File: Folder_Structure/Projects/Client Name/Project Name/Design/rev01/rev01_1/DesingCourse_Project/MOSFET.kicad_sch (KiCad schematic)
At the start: 0 parts

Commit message: Update 6
SCH and LIB for MOSFET page done, missing passive components
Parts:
- added C42, C43: 2n2, symbol Device:C
- added J4, J5, J6: 7461084, WP-BUTR:WP-BUTR_7461084, symbol 7461084:WP-7461084
- added NT2, NT3, NT4, NT5: NetTie_2, symbol Device:NetTie_2
- added Q1, Q2, Q3, Q4, Q5, Q6: HSBA15810C, Package_SO:PowerPAK_SO-8_Single, symbol HSBA15810C:HSBA15810C
- added R24, R26, R30, R31, R36, R37: 4R7, symbol Device:R
- added R25, R32, R38: 39K, symbol Device:R
- added R27, R28, R33, R34: 100, symbol Device:R
- added R29, R35: 1m, RES_WSLP2726L5000FEA:WSLP2726_1mOHM_VIS, symbol WSLP27261L000FEA:WSLP27261L000FEA
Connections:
- new net +VDC: Q1.5 (D), Q3.5 (D), Q5.5 (D)
- new net GND: NT5.1, R25.2, R29.2, R32.2, R35.2, R38.2
- new net H1_LOW: Q2.1 (S), Q2.2 (S), Q2.3 (S), R29.1
- new net H1_VS: NT2.1
- new net H2_LOW: Q4.1 (S), Q4.2 (S), Q4.3 (S), R35.1
- new net H2_VS: NT3.1
- new net H3_LOW: NT5.2, Q6.1 (S), Q6.2 (S), Q6.3 (S)
- new net H3_VS: NT4.1
- new net M_H1: R24.1
- new net M_H1_RG: Q1.4 (G), R24.2
- new net M_H2: R30.1
- new net M_H2_RG: Q3.4 (G), R30.2
- new net M_H3: R36.1
- new net M_H3_RG: Q5.4 (G), R36.2
- new net M_L1: R26.1
- new net M_L1_RG: Q2.4 (G), R25.1, R26.2
- new net M_L2: R31.1
- new net M_L2_RG: Q4.4 (G), R31.2, R32.1
- new net M_L3: R37.1
- new net M_L3_RG: Q6.4 (G), R37.2, R38.1
- new net PHASE_1: J4.1, J4.2, J4.3, J4.4, J4.5, J4.6, J4.7, J4.8, NT2.2, Q1.1 (S), Q1.2 (S), Q1.3 (S), Q2.5 (D)
- new net PHASE_2: J5.1, J5.2, J5.3, J5.4, J5.5, J5.6, J5.7, J5.8, NT3.2, Q3.1 (S), Q3.2 (S), Q3.3 (S), Q4.5 (D)
- new net PHASE_3: J6.1, J6.2, J6.3, J6.4, J6.5, J6.6, J6.7, J6.8, NT4.2, Q5.1 (S), Q5.2 (S), Q5.3 (S), Q6.5 (D)
- new net S1_N: C42.1, R27.1
- new net S1_P: C42.2, R28.1
- new net S2_N: C43.1, R33.1
- new net S2_P: C43.2, R34.1
- new net SH1_N: R27.2, R29.3
- new net SH1_P: R28.2, R29.4
- new net SH2_N: R33.2, R35.3
- new net SH2_P: R34.2, R35.4
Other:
- note added: "H#_VS"
- note added: "Kelving connection for sensing"
- note added: "M6 screw terminal"
- note added: "MCU SENSING FEEDBACK FOR EACH PHASE"
- note added: "MOSFETs"
- note added: "OUTPUT PHASE 1"
- note added: "OUTPUT PHASE 2"
- note added: "OUTPUT PHASE 3"
- note added: "Phase 1"
- note added: "Phase 2"
- note added: "Phase 3"
- note added: "Place as close as possible to the bulk capacitanace"
- note added: "Q_CONTROL"
- note added: "Q_SOURCES"
- note added: "SENSE L1"
- note added: "SENSE L2"
- company: (none) -> Integro Consulting AB
- title: (none) -> PCB Mastery Project

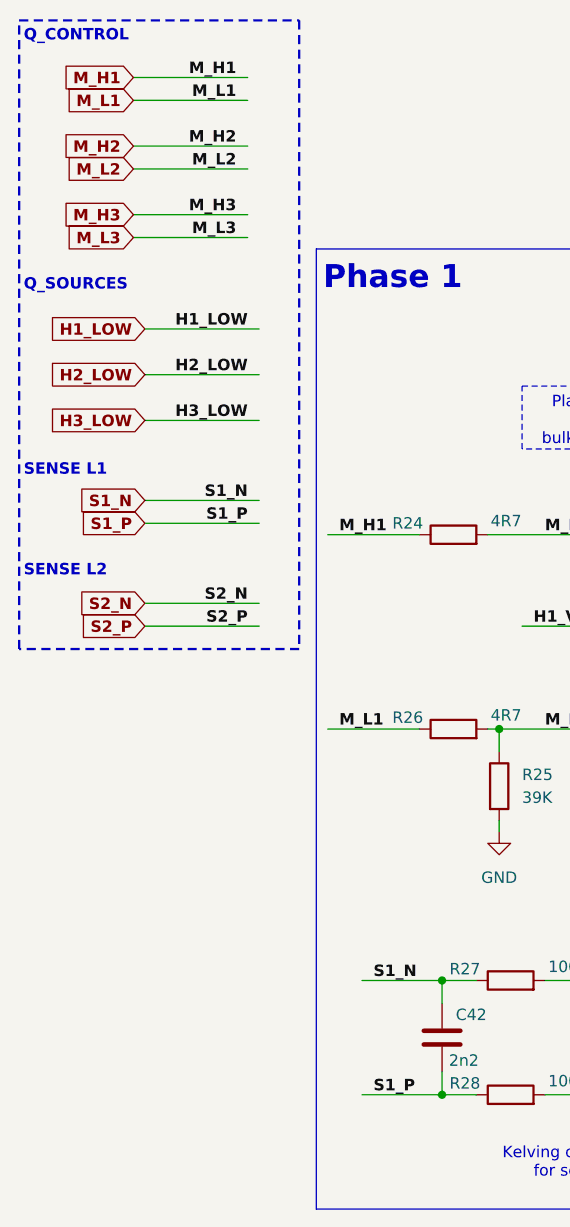
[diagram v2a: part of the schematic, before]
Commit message: Update 10
All done up to MOSFET page, replace all connected to actual PN
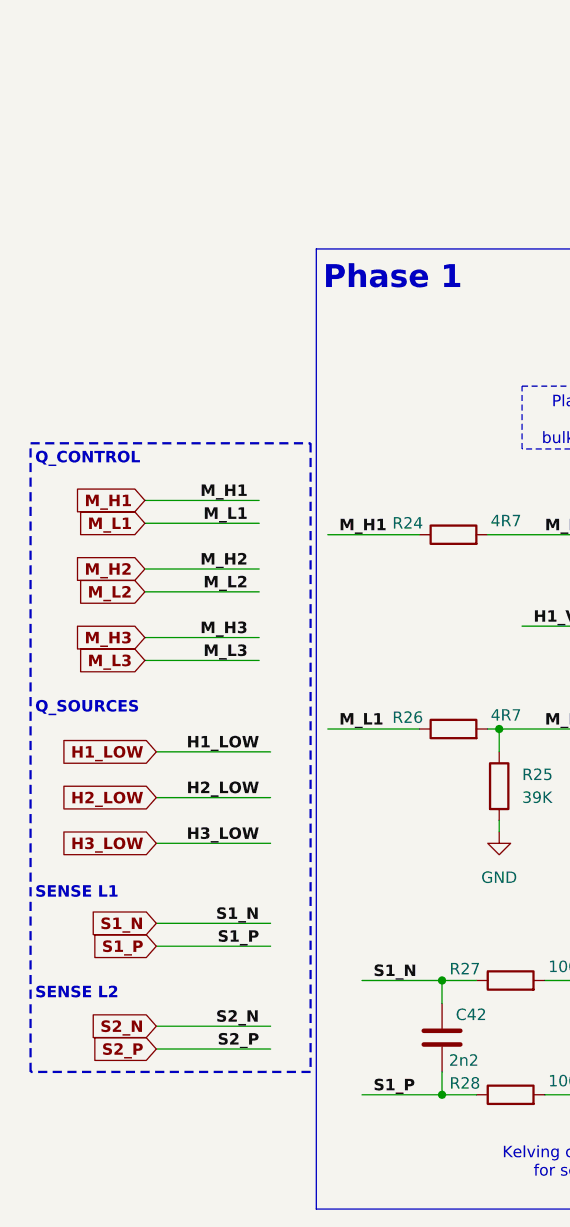
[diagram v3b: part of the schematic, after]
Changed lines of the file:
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@@
 	)
 	(rectangle
-		(start 12.7 12.7)
-		(end 43.815 82.55)
+		(start 13.97 59.69)
+		(end 45.085 129.54)
 		(stroke
 			(width 0.254)
@@
 	(text "Q_CONTROL"
 		(exclude_from_sim no)
-		(at 13.208 14.478 0)
+		(at 14.478 61.468 0)
 		(effects
 			(font
@@
 	(text "Q_SOURCES\n"
 		(exclude_from_sim no)
-		(at 13.208 42.164 0)
+		(at 14.478 89.154 0)
 		(effects
 			(font
@@
 	(text "SENSE L1"
 		(exclude_from_sim no)
-		(at 13.208 62.738 0)
+		(at 14.478 109.728 0)
 		(effects
 			(font
@@
 	(text "SENSE L2\n"
 		(exclude_from_sim no)
-		(at 13.208 73.914 0)
+		(at 14.478 120.904 0)
 		(effects
 			(font
@@
 	(wire
 		(pts
-			(xy 39.37 66.04) (xy 26.67 66.04)
+			(xy 40.64 113.03) (xy 27.94 113.03)
 		)
 		(stroke
@@
 	(wire
 		(pts
-			(xy 38.1 26.67) (xy 25.4 26.67)
+			(xy 39.37 73.66) (xy 26.67 73.66)
 		)
 		(stroke
@@
 	(wire
 		(pts
-			(xy 38.1 21.59) (xy 25.4 21.59)
+			(xy 39.37 68.58) (xy 26.67 68.58)
 		)
 		(stroke
@@
 	(wire
 		(pts
-			(xy 38.1 19.05) (xy 25.4 19.05)
+			(xy 39.37 66.04) (xy 26.67 66.04)
 		)
 		(stroke
@@
 	(wire
 		(pts
-			(xy 39.37 57.15) (xy 26.67 57.15)
+			(xy 40.64 104.14) (xy 27.94 104.14)
 		)
 		(stroke
@@
 	(wire
 		(pts
-			(xy 39.37 46.99) (xy 26.67 46.99)
+			(xy 40.64 93.98) (xy 27.94 93.98)
 		)
 		(stroke
@@
 	(wire
 		(pts
-			(xy 39.37 68.58) (xy 26.67 68.58)
+			(xy 40.64 115.57) (xy 27.94 115.57)
 		)
 		(stroke
@@
 	(wire
 		(pts
-			(xy 38.1 29.21) (xy 25.4 29.21)
+			(xy 39.37 76.2) (xy 26.67 76.2)
 		)
 		(stroke
@@
 	(wire
 		(pts
-			(xy 38.1 34.29) (xy 25.4 34.29)
+			(xy 39.37 81.28) (xy 26.67 81.28)
 		)
 		(stroke
@@
 	(wire
 		(pts
-			(xy 39.37 77.47) (xy 26.67 77.47)
+			(xy 40.64 124.46) (xy 27.94 124.46)
 		)
 		(stroke
@@
 	(wire
 		(pts
-			(xy 39.37 52.07) (xy 26.67 52.07)
+			(xy 40.64 99.06) (xy 27.94 99.06)
 		)
 		(stroke
@@
 	(wire
 		(pts
-			(xy 38.1 36.83) (xy 25.4 36.83)
+			(xy 39.37 83.82) (xy 26.67 83.82)
 		)
 		(stroke
@@
 	(wire
 		(pts
-			(xy 39.37 80.01) (xy 26.67 80.01)
+			(xy 40.64 127) (xy 27.94 127)
 		)
 		(stroke
@@
 	)
 	(label "H2_LOW"
-		(at 38.1 52.07 180)
+		(at 39.37 99.06 180)
 		(effects
 			(font
@@
 	)
 	(label "M_L1"
-		(at 36.83 21.59 180)
+		(at 38.1 68.58 180)
 		(effects
 			(font
@@
 	)
 	(label "H3_LOW"
-		(at 38.1 57.15 180)
+		(at 39.37 104.14 180)
 		(effects
 			(font
@@
 	)
 	(label "M_H1"
-		(at 36.83 19.05 180)
+		(at 38.1 66.04 180)
 		(effects
 			(font
@@
 	)
 	(label "S1_N"
-		(at 38.1 66.04 180)
+		(at 39.37 113.03 180)
 		(effects
 			(font
@@
 	)
 	(label "S2_N"
-		(at 38.1 77.47 180)
+		(at 39.37 124.46 180)
 		(effects
 			(font
@@
 	)
 	(label "S2_P"
-		(at 38.1 80.01 180)
+		(at 39.37 127 180)
 		(effects
 			(font
@@
 	)
 	(label "M_H2"
-		(at 36.83 26.67 180)
+		(at 38.1 73.66 180)
 		(effects
 			(font
@@
 	)
 	(label "M_H3"
-		(at 36.83 34.29 180)
+		(at 38.1 81.28 180)
 		(effects
 			(font
@@
 	)
 	(label "M_L3"
-		(at 36.83 36.83 180)
+		(at 38.1 83.82 180)
 		(effects
 			(font
@@
 	)
 	(label "H1_LOW"
-		(at 38.1 46.99 180)
+		(at 39.37 93.98 180)
 		(effects
 			(font
@@
 	)
 	(label "S1_P"
-		(at 38.1 68.58 180)
+		(at 39.37 115.57 180)
 		(effects
 			(font
@@
 	)
 	(label "M_L2"
-		(at 36.83 29.21 180)
+		(at 38.1 76.2 180)
 		(effects
 			(font
@@
 	(global_label "M_L1"
 		(shape input)
-		(at 25.4 21.59 180)
+		(at 26.67 68.58 180)
 		(fields_autoplaced yes)
 		(effects
@@
 		)
 		(property "Intersheetrefs" "${INTERSHEET_REFS}"
-			(at 17.1871 21.59 0)
+			(at 18.4571 68.58 0)
 			(effects
 				(font
@@
 	(global_label "S2_P"
 		(shape input)
-		(at 26.67 80.01 180)
+		(at 27.94 127 180)
 		(fields_autoplaced yes)
 		(effects
@@
 		)
 		(property "Intersheetrefs" "${INTERSHEET_REFS}"
-			(at 18.4571 80.01 0)
+			(at 19.7271 127 0)
 			(effects
 				(font
@@
 	(global_label "H2_LOW"
 		(shape input)
-		(at 26.67 52.07 180)
+		(at 27.94 99.06 180)
 		(fields_autoplaced yes)
 		(effects
@@
 		)
 		(property "Intersheetrefs" "${INTERSHEET_REFS}"
-			(at 15.7961 52.07 0)
+			(at 17.0661 99.06 0)
 			(effects
 				(font
@@
 	(global_label "M_H3"
 		(shape input)
-		(at 25.4 34.29 180)
+		(at 26.67 81.28 180)
 		(fields_autoplaced yes)
 		(effects
@@
 		)
 		(property "Intersheetrefs" "${INTERSHEET_REFS}"
-			(at 16.8847 34.29 0)
+			(at 18.1547 81.28 0)
 			(effects
 				(font
@@
 	(global_label "H3_LOW"
 		(shape input)
-		(at 26.67 57.15 180)
+		(at 27.94 104.14 180)
 		(fields_autoplaced yes)
 		(effects
@@
 		)
 		(property "Intersheetrefs" "${INTERSHEET_REFS}"
-			(at 15.7961 57.15 0)
+			(at 17.0661 104.14 0)
 			(effects
 				(font
@@
 	(global_label "S2_N"
 		(shape input)
-		(at 26.67 77.47 180)
+		(at 27.94 124.46 180)
 		(fields_autoplaced yes)
 		(effects
@@
 		)
 		(property "Intersheetrefs" "${INTERSHEET_REFS}"
-			(at 18.3966 77.47 0)
+			(at 19.6666 124.46 0)
 			(effects
 				(font
@@
 	(global_label "S1_N"
 		(shape input)
-		(at 26.67 66.04 180)
+		(at 27.94 113.03 180)
 		(fields_autoplaced yes)
 		(effects
@@
 		)
 		(property "Intersheetrefs" "${INTERSHEET_REFS}"
-			(at 18.3966 66.04 0)
+			(at 19.6666 113.03 0)
 			(effects
 				(font
@@
 	(global_label "M_H2"
 		(shape input)
-		(at 25.4 26.67 180)
+		(at 26.67 73.66 180)
 		(fields_autoplaced yes)
 		(effects
@@
 		)
 		(property "Intersheetrefs" "${INTERSHEET_REFS}"
-			(at 16.8847 26.67 0)
+			(at 18.1547 73.66 0)
 			(effects
 				(font
@@
 	(global_label "M_L3"
 		(shape input)
-		(at 25.4 36.83 180)
+		(at 26.67 83.82 180)
 		(fields_autoplaced yes)
 		(effects
@@
 		)
 		(property "Intersheetrefs" "${INTERSHEET_REFS}"
-			(at 17.1871 36.83 0)
+			(at 18.4571 83.82 0)
 			(effects
 				(font
@@
 	(global_label "H1_LOW"
 		(shape input)
-		(at 26.67 46.99 180)
+		(at 27.94 93.98 180)
 		(fields_autoplaced yes)
 		(effects
@@
 		)
 		(property "Intersheetrefs" "${INTERSHEET_REFS}"
-			(at 15.7961 46.99 0)
+			(at 17.0661 93.98 0)
 			(effects
 				(font
@@
 	(global_label "M_H1"
 		(shape input)
-		(at 25.4 19.05 180)
+		(at 26.67 66.04 180)
 		(fields_autoplaced yes)
 		(effects
@@
 		)
 		(property "Intersheetrefs" "${INTERSHEET_REFS}"
-			(at 16.8847 19.05 0)
+			(at 18.1547 66.04 0)
 			(effects
 				(font
@@
 	(global_label "S1_P"
 		(shape input)
-		(at 26.67 68.58 180)
+		(at 27.94 115.57 180)
 		(fields_autoplaced yes)
 		(effects
@@
 		)
 		(property "Intersheetrefs" "${INTERSHEET_REFS}"
-			(at 18.4571 68.58 0)
+			(at 19.7271 115.57 0)
 			(effects
 				(font
@@
 	(global_label "M_L2"
 		(shape input)
-		(at 25.4 29.21 180)
+		(at 26.67 76.2 180)
 		(fields_autoplaced yes)
 		(effects
@@
 		)
 		(property "Intersheetrefs" "${INTERSHEET_REFS}"
-			(at 17.1871 29.21 0)
+			(at 18.4571 76.2 0)
 			(effects
 				(font

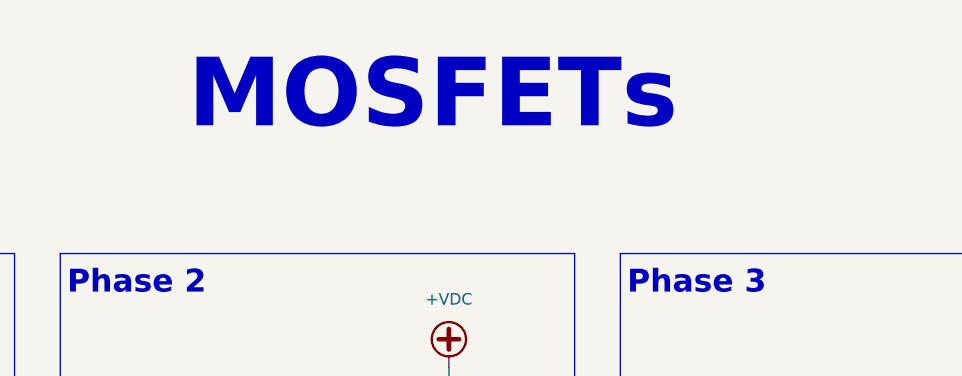
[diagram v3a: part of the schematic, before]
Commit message: Update 11
SCH finishe, missing the labels and logos and adding all passive components
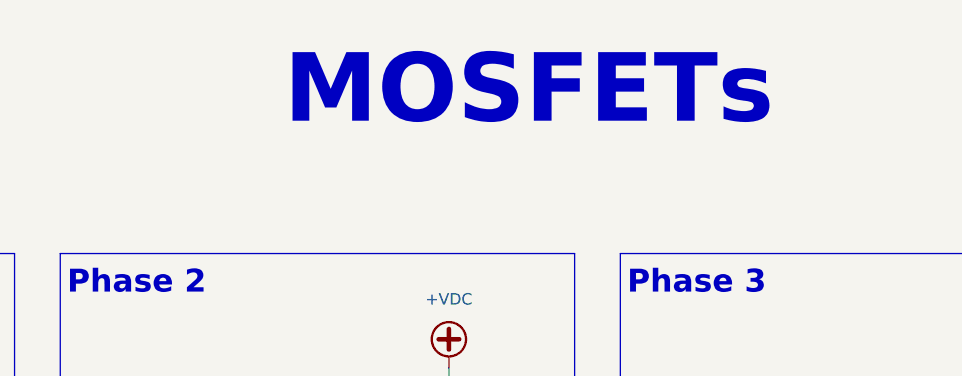
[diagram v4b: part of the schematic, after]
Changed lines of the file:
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@@
 	(text "MOSFETs\n"
 		(exclude_from_sim no)
-		(at 149.352 20.574 0)
+		(at 160.02 20.066 0)
 		(effects
 			(font

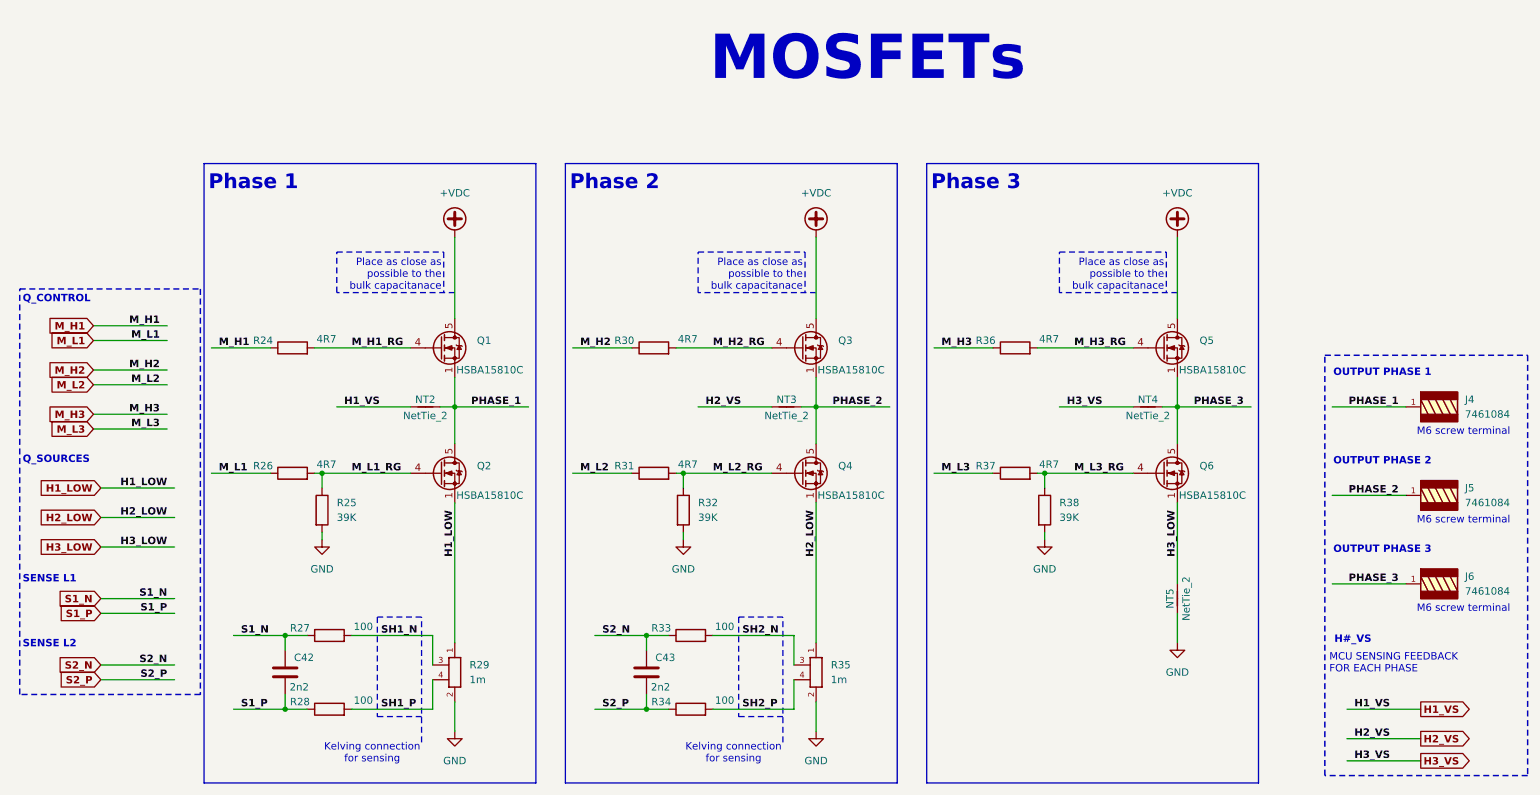
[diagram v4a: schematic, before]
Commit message: Update 12
Until STEP-DOWN page, all components have complete libraries.

Creation and incluison of all logos and labels libraries
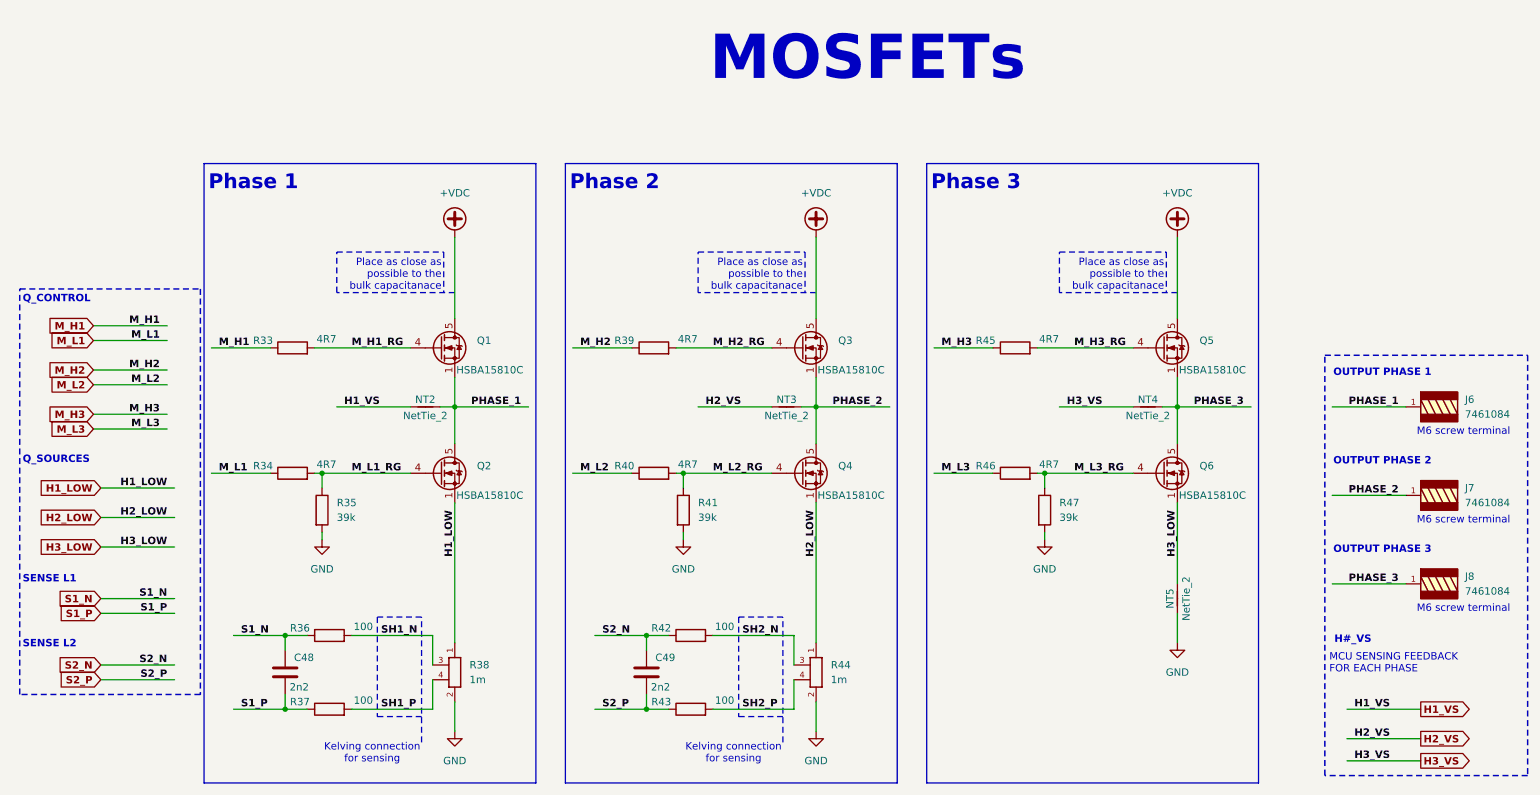
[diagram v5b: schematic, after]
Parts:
- removed R25, R32, R38: 39K, symbol Device:R
- added R35, R41, R47: 39k, Resistor_SMD:R_0603_1608Metric, symbol Device:R
- renumbered C42 to C48, C43 to C49, J4 to J6, J5 to J7, J6 to J8, R24 to R33, R26 to R34, R27 to R36, R28 to R37, R29 to R38, R30 to R39, R31 to R40, R33 to R42, R34 to R43, R35 to R44, R36 to R45, R37 to R46
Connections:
- net GND: now also R35.2, R41.2, R47.2
- net M_L1_RG: now also R35.1
- net M_L2_RG: now also R41.1
- net M_L3_RG: now also R47.1

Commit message: Update14
All components with FP, missing the block diagram
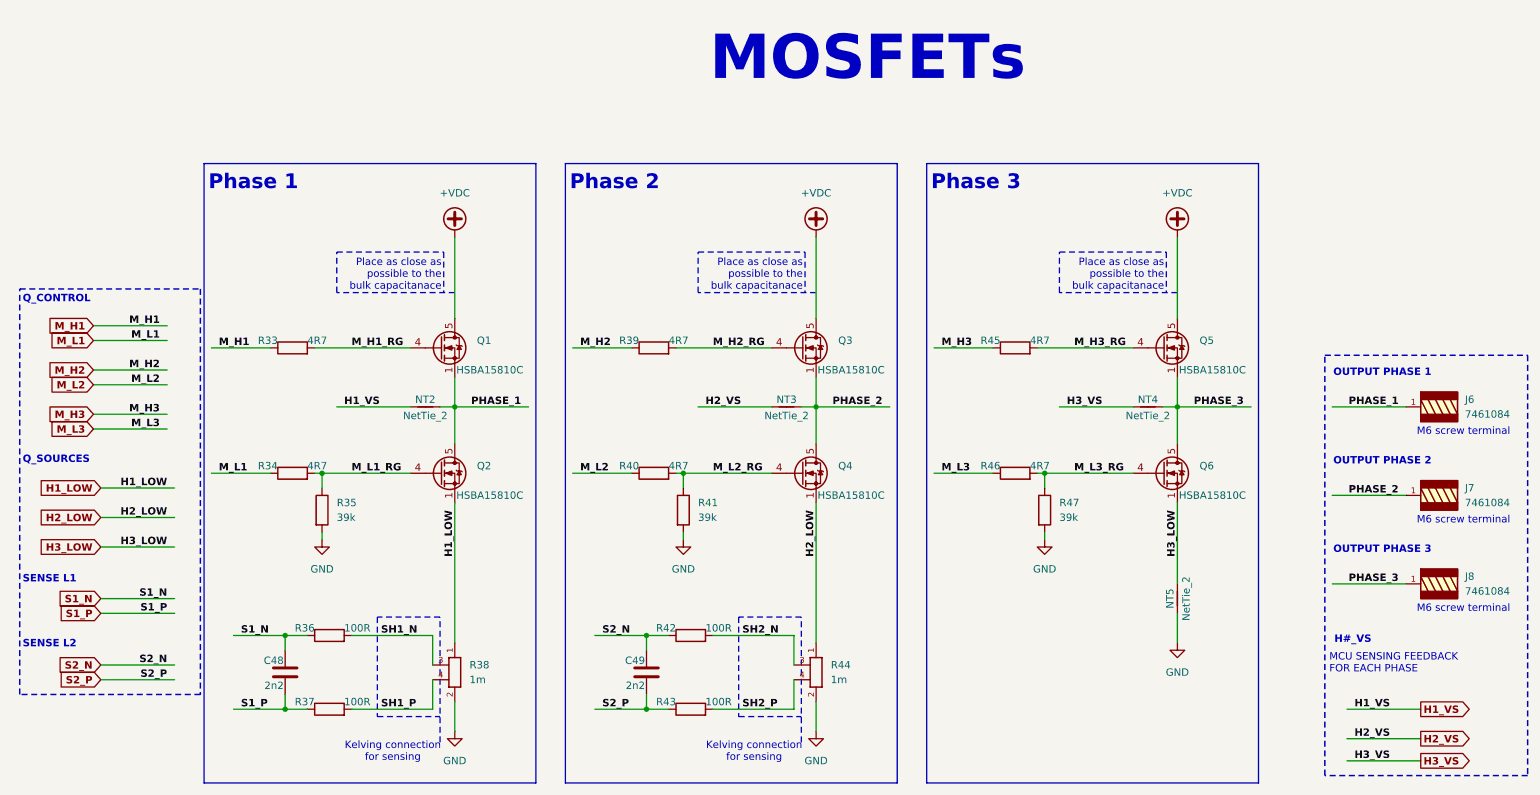
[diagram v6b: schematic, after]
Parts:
- C48, C49: footprint (none) -> Capacitor_SMD:C_0603_1608Metric; Package (none) -> 0603; Temp Coeff (none) -> X7R; Tolerance (none) -> 10%; Voltage Rating (none) -> 100V
- NT2, NT3, NT4, NT5: footprint (none) -> NetTie:NetTie-2_SMD_Pad0.5mm
- R33, R34, R39, R40, R45, R46: footprint (none) -> Resistor_SMD:R_0603_1608Metric; Package (none) -> 0603; Power Rating (none) -> 1/10W; Tolerance (none) -> 1%
- R36, R37, R42, R43: value 100 -> 100R; footprint (none) -> Resistor_SMD:R_0603_1608Metric; Package (none) -> 0603; Power Rating (none) -> 1/10W; Tolerance (none) -> 1%
